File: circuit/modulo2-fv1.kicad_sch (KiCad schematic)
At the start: 67 parts, among them J1 CONN_01X04, J2 POWER, J3 CONN_01X02, J4 HOLE, J5 HOLE, J6 USB_OTG, SW1 ROTENC_BOURNS_PEL12D, U1 NE5532, U10 TLE2426, U3 FV-1, U4 AVR-ISP6, U5 LM1117 3V3, U6 ATmega328p, U7 DBG_UART, U8 74164, Y1 16MHz

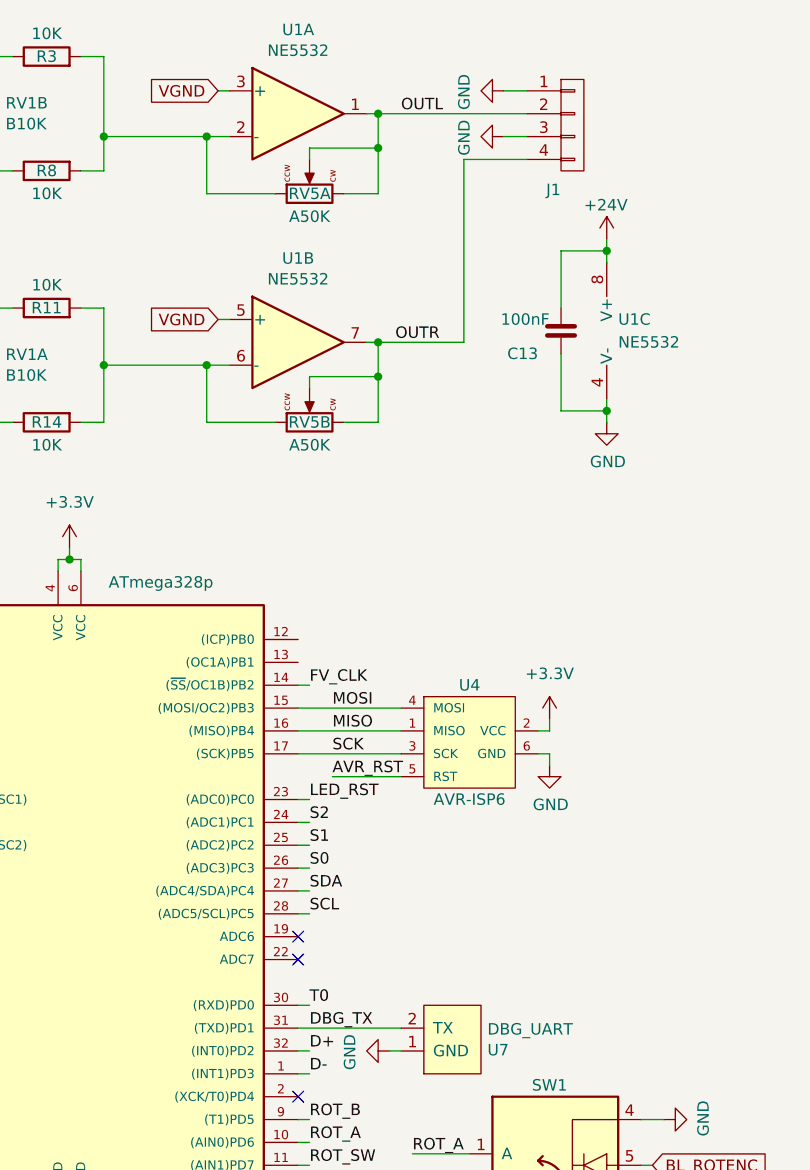
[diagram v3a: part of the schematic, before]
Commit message: further routing of FV-1
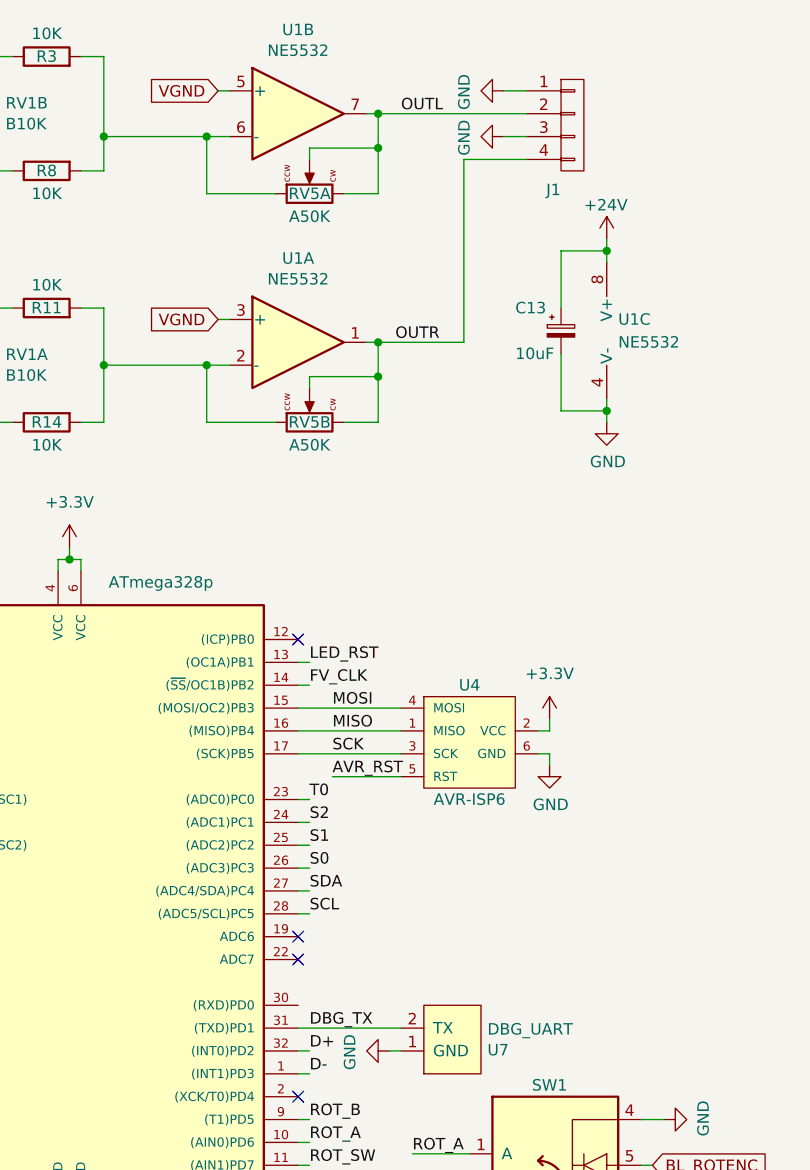
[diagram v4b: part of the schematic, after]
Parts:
- removed C13: 100nF, myAmp:C_5MM_1206, symbol myAmp:C
- added C13: 10uF, myAmp:CPOL_D6.3_P2.5, symbol myAmp:CPOL
- C2: footprint myAmp:C_FILM_L7.2mm_W4.5mm_P5.00mm -> myAmp:C_FILM_L7.2mm_W5.0mm_P5.00mm
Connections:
- net +24V: now also C13.1
- net GND: now also C13.2
- net LED_RST: now also U6.13 ((OC1A)PB1); no longer U6.23 ((ADC0)PC0)
- net OUTL: now also U1.7; no longer U1.1
- net OUTR: now also U1.1; no longer U1.7
- net T0: now also U6.23 ((ADC0)PC0); no longer U6.30 ((RXD)PD0)
- net at R3.2, R8.2, RV5.1: now also U1.6 (-); no longer U1.2 (-)
- net at R11.2, R14.2, RV5.4 (1): now also U1.2 (-); no longer U1.6 (-)
- no-connect marks 11 -> 12
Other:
- moved on the sheet: U1A, U1B
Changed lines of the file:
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@@
   (no_connect (at 128.27 162.56))
   (no_connect (at 128.27 172.72))
+  (no_connect (at 232.41 81.28))
   (no_connect (at 232.41 114.3))
   (no_connect (at 232.41 116.84))
@@
     (stroke (width 0) (type default) (color 0 0 0 0))
   )
-  (wire (pts (xy 233.68 99.06) (xy 232.41 99.06))
+  (wire (pts (xy 233.68 83.82) (xy 232.41 83.82))
     (stroke (width 0) (type default) (color 0 0 0 0))
   )
@@
     (stroke (width 0) (type default) (color 0 0 0 0))
   )
-  (wire (pts (xy 233.68 121.92) (xy 232.41 121.92))
+  (wire (pts (xy 233.68 99.06) (xy 232.41 99.06))
     (stroke (width 0) (type default) (color 0 0 0 0))
   )
@@
     (effects (font (size 1.27 1.27)) (justify left bottom))
   )
-  (label "T0" (at 233.68 121.92 0)
+  (label "T0" (at 233.68 99.06 0)
     (effects (font (size 1.27 1.27)) (justify left bottom))
   )
@@
     (effects (font (size 1.27 1.27)) (justify left bottom))
   )
-  (label "LED_RST" (at 233.68 99.06 0)
+  (label "LED_RST" (at 233.68 83.82 0)
     (effects (font (size 1.27 1.27)) (justify left bottom))
   )
@@
       (effects (font (size 1.27 1.27)) (justify right))
     )
-    (property "Footprint" "myAmp:C_FILM_L7.2mm_W4.5mm_P5.00mm" (id 2) (at 34.29 18.0848 0)
+    (property "Footprint" "myAmp:C_FILM_L7.2mm_W5.0mm_P5.00mm" (id 2) (at 34.29 18.0848 0)
       (effects (font (size 1.27 1.27)) hide)
     )
@@
     (pin "2")
   )
+  (symbol (lib_id "myAmp:CPOL") (at 261.62 46.99 0) (unit 1)
+    (in_bom yes) (on_board yes)
+    (property "Reference" "C13" (id 0) (at 256.54 44.45 0)
+      (effects (font (size 1.27 1.27)) (justify left))
+    )
+    (property "Value" "10uF" (id 1) (at 256.54 49.53 0)
+      (effects (font (size 1.27 1.27)) (justify left))
+    )
+    (property "Footprint" "myAmp:CPOL_D6.3_P2.5" (id 2) (at 261.62 46.99 0)
+      (effects (font (size 1.27 1.27)) hide)
+    )
+    (property "Datasheet" "" (id 3) (at 261.62 46.99 0)
+      (effects (font (size 1.27 1.27)) hide)
+    )
+    (pin "1")
+    (pin "2")
+  )
   (symbol (lib_id "myAmp:CONN_01X04") (at 262.89 24.13 0) (unit 1)
     (in_bom yes) (on_board yes)
@@
     (pin "8")
   )
-  (symbol (lib_id "myAmp:C") (at 261.62 46.99 0) (mirror x) (unit 1)
-    (in_bom yes) (on_board yes)
-    (property "Reference" "C13" (id 0) (at 259.08 49.53 0)
-      (effects (font (size 1.27 1.27)) (justify right))
-    )
-    (property "Value" "100nF" (id 1) (at 260.35 45.72 0)
-      (effects (font (size 1.27 1.27)) (justify right))
-    )
-    (property "Footprint" "myAmp:C_5MM_1206" (id 2) (at 262.5852 43.18 0)
-      (effects (font (size 1.27 1.27)) hide)
-    )
-    (property "Datasheet" "" (id 3) (at 261.62 46.99 0)
-      (effects (font (size 1.27 1.27)) hide)
-    )
-    (pin "1")
-    (pin "2")
-  )
   (symbol (lib_id "power:+3.3V") (at 133.35 154.94 0) (unit 1)
     (in_bom yes) (on_board yes) (fields_autoplaced)
@@
     (pin "2")
   )
-  (symbol (lib_id "myAmp:TL072") (at 232.41 22.86 0) (unit 1)
+  (symbol (lib_id "myAmp:TL072") (at 232.41 48.26 0) (unit 1)
     (in_bom yes) (on_board yes)
-    (property "Reference" "U1" (id 0) (at 232.41 13.5382 0))
-    (property "Value" "NE5532" (id 1) (at 232.41 15.8496 0))
-    (property "Footprint" "myAmp:SOIC-8_3.9x4.9mm_P1.27mm" (id 2) (at 232.41 22.86 0)
+    (property "Reference" "U1" (id 0) (at 232.41 38.9382 0))
+    (property "Value" "NE5532" (id 1) (at 232.41 41.2496 0))
+    (property "Footprint" "myAmp:SOIC-8_3.9x4.9mm_P1.27mm" (id 2) (at 232.41 48.26 0)
       (effects (font (size 1.27 1.27)) hide)
     )
-    (property "Datasheet" "" (id 3) (at 232.41 22.86 0)
+    (property "Datasheet" "" (id 3) (at 232.41 48.26 0)
       (effects (font (size 1.27 1.27)) hide)
     )
@@
     (pin "1")
   )
-  (symbol (lib_id "myAmp:TL072") (at 232.41 48.26 0) (unit 2)
+  (symbol (lib_id "myAmp:TL072") (at 232.41 22.86 0) (unit 2)
     (in_bom yes) (on_board yes)
-    (property "Reference" "U1" (id 0) (at 232.41 38.9382 0))
-    (property "Value" "NE5532" (id 1) (at 232.41 41.2496 0))
-    (property "Footprint" "myAmp:SOIC-8_3.9x4.9mm_P1.27mm" (id 2) (at 232.41 48.26 0)
+    (property "Reference" "U1" (id 0) (at 232.41 13.5382 0))
+    (property "Value" "NE5532" (id 1) (at 232.41 15.8496 0))
+    (property "Footprint" "myAmp:SOIC-8_3.9x4.9mm_P1.27mm" (id 2) (at 232.41 22.86 0)
       (effects (font (size 1.27 1.27)) hide)
     )
-    (property "Datasheet" "" (id 3) (at 232.41 48.26 0)
+    (property "Datasheet" "" (id 3) (at 232.41 22.86 0)
       (effects (font (size 1.27 1.27)) hide)
     )
@@
     )
     (path "/00000000-0000-0000-0000-00005ef231e4"
-      (reference "C2") (unit 1) (value "1µF") (footprint "myAmp:C_FILM_L7.2mm_W4.5mm_P5.00mm")
+      (reference "C2") (unit 1) (value "1µF") (footprint "myAmp:C_FILM_L7.2mm_W5.0mm_P5.00mm")
     )
     (path "/00000000-0000-0000-0000-00005ef231f9"
@@
       (reference "C12") (unit 1) (value "100nF") (footprint "myAmp:C_1206")
     )
-    (path "/a9a1d56b-2c01-49af-987b-e5fe275248ce"
-      (reference "C13") (unit 1) (value "100nF") (footprint "myAmp:C_5MM_1206")
+    (path "/1dfd57e6-2750-423f-b47b-e3e12643c855"
+      (reference "C13") (unit 1) (value "10uF") (footprint "myAmp:CPOL_D6.3_P2.5")
     )
     (path "/3cd1ca54-876a-4df6-8500-19a372da4c45"

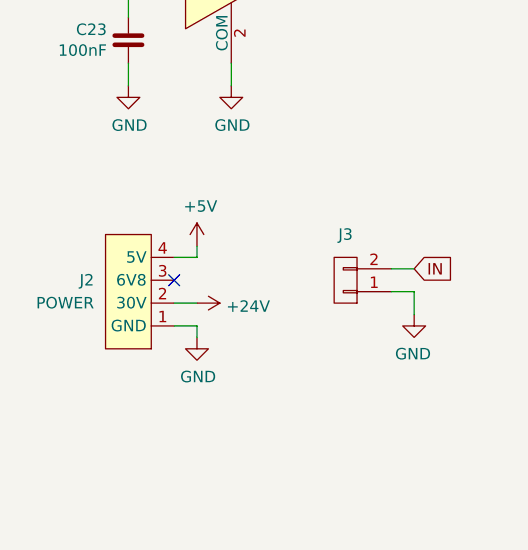
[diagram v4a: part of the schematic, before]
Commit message: no more assembler; more routing
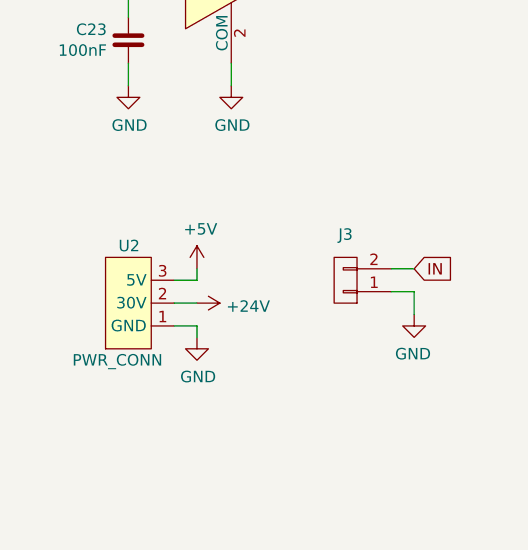
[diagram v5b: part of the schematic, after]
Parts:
- removed J2: POWER, myAmp:POWER, symbol myAmp:POWER
- added U2: PWR_CONN, myAmp:PWR_CONN, symbol myAmp:PWR_CONN
- C23: footprint myAmp:C_1206 -> myAmp:C_5MM_1206
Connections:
- net +24V: now also U2.2 (30V)
- net +5V: now also U2.3 (5V)
- net GND: now also U2.1 (GND)
- no-connect marks 12 -> 11
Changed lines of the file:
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@@
   (junction (at 152.4 106.68) (diameter 0) (color 0 0 0 0)
   )
-  (no_connect (at 30.48 167.64))
   (no_connect (at 162.56 193.04))
   (no_connect (at 162.56 187.96))
@@
     (stroke (width 0) (type default) (color 0 0 0 0))
   )
-  (wire (pts (xy 30.48 165.1) (xy 33.02 165.1))
+  (wire (pts (xy 30.48 167.64) (xy 33.02 167.64))
     (stroke (width 0) (type default) (color 0 0 0 0))
   )
@@
     (stroke (width 0) (type default) (color 0 0 0 0))
   )
-  (wire (pts (xy 33.02 165.1) (xy 33.02 163.83))
+  (wire (pts (xy 33.02 167.64) (xy 33.02 166.37))
     (stroke (width 0) (type default) (color 0 0 0 0))
   )
@@
       (effects (font (size 1.27 1.27)) (justify right))
     )
-    (property "Footprint" "myAmp:C_1206" (id 2) (at 26.3652 137.16 0)
+    (property "Footprint" "myAmp:C_5MM_1206" (id 2) (at 26.3652 137.16 0)
       (effects (font (size 1.27 1.27)) hide)
     )
@@
     (pin "1")
   )
-  (symbol (lib_id "power:+5V") (at 33.02 163.83 0) (unit 1)
+  (symbol (lib_id "power:+5V") (at 33.02 166.37 0) (unit 1)
     (in_bom yes) (on_board yes)
-    (property "Reference" "#PWR037" (id 0) (at 33.02 167.64 0)
+    (property "Reference" "#PWR037" (id 0) (at 33.02 170.18 0)
       (effects (font (size 1.27 1.27)) hide)
     )
-    (property "Value" "+5V" (id 1) (at 33.401 159.4358 0))
-    (property "Footprint" "" (id 2) (at 33.02 163.83 0)
+    (property "Value" "+5V" (id 1) (at 33.401 161.9758 0))
+    (property "Footprint" "" (id 2) (at 33.02 166.37 0)
       (effects (font (size 1.27 1.27)) hide)
     )
-    (property "Datasheet" "" (id 3) (at 33.02 163.83 0)
+    (property "Datasheet" "" (id 3) (at 33.02 166.37 0)
       (effects (font (size 1.27 1.27)) hide)
     )
@@
     (pin "1")
   )
+  (symbol (lib_id "myAmp:PWR_CONN") (at 26.67 170.18 0) (mirror x) (unit 1)
+    (in_bom yes) (on_board yes)
+    (property "Reference" "U2" (id 0) (at 26.67 163.83 0)
+      (effects (font (size 1.27 1.27)) (justify right))
+    )
+    (property "Value" "PWR_CONN" (id 1) (at 29.21 176.53 0)
+      (effects (font (size 1.27 1.27)) (justify right))
+    )
+    (property "Footprint" "myAmp:PWR_CONN" (id 2) (at 29.21 168.91 0)
+      (effects (font (size 1.27 1.27)) hide)
+    )
+    (property "Datasheet" "" (id 3) (at 29.21 168.91 0)
+      (effects (font (size 1.27 1.27)) hide)
+    )
+    (pin "1")
+    (pin "2")
+    (pin "3")
+  )
   (symbol (lib_id "myAmp:R") (at 204.47 44.45 90) (unit 1)
     (in_bom yes) (on_board yes)
@@
     (pin "1")
   )
-  (symbol (lib_id "myAmp:POWER") (at 26.67 168.91 0) (mirror x) (unit 1)
-    (in_bom yes) (on_board yes) (fields_autoplaced)
-    (property "Reference" "J2" (id 0) (at 21.59 167.6399 0)
-      (effects (font (size 1.27 1.27)) (justify right))
-    )
-    (property "Value" "POWER" (id 1) (at 21.59 170.1799 0)
-      (effects (font (size 1.27 1.27)) (justify right))
-    )
-    (property "Footprint" "myAmp:POWER" (id 2) (at 29.21 168.91 0)
-      (effects (font (size 1.27 1.27)) hide)
-    )
-    (property "Datasheet" "" (id 3) (at 29.21 168.91 0)
-      (effects (font (size 1.27 1.27)) hide)
-    )
-    (pin "1")
-    (pin "2")
-    (pin "3")
-    (pin "4")
-  )
   (symbol (lib_id "power:+3.3V") (at 260.35 90.17 0) (unit 1)
     (in_bom yes) (on_board yes) (fields_autoplaced)
@@
     )
     (path "/00000000-0000-0000-0000-000061a5277b"
-      (reference "C23") (unit 1) (value "100nF") (footprint "myAmp:C_1206")
+      (reference "C23") (unit 1) (value "100nF") (footprint "myAmp:C_5MM_1206")
     )
     (path "/00000000-0000-0000-0000-00005ef2310d"
@@
       (reference "J1") (unit 1) (value "CONN_01X04") (footprint "myAmp:PIN_1x04")
     )
-    (path "/51d5e13b-3b49-4f7b-9b29-66809d04819d"
-      (reference "J2") (unit 1) (value "POWER") (footprint "myAmp:POWER")
-    )
     (path "/28815f0f-6ffd-4c35-80d2-568c37ba7f80"
       (reference "J3") (unit 1) (value "CONN_01X02") (footprint "myAmp:PIN_1x02")
@@
       (reference "U1") (unit 3) (value "NE5532") (footprint "myAmp:SOIC-8_3.9x4.9mm_P1.27mm")
     )
+    (path "/1bbee457-a6b3-4f68-8607-daa9c3f4a984"
+      (reference "U2") (unit 1) (value "PWR_CONN") (footprint "myAmp:PWR_CONN")
+    )
     (path "/00000000-0000-0000-0000-00005ef23204"
